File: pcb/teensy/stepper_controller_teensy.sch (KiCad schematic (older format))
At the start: 22 parts

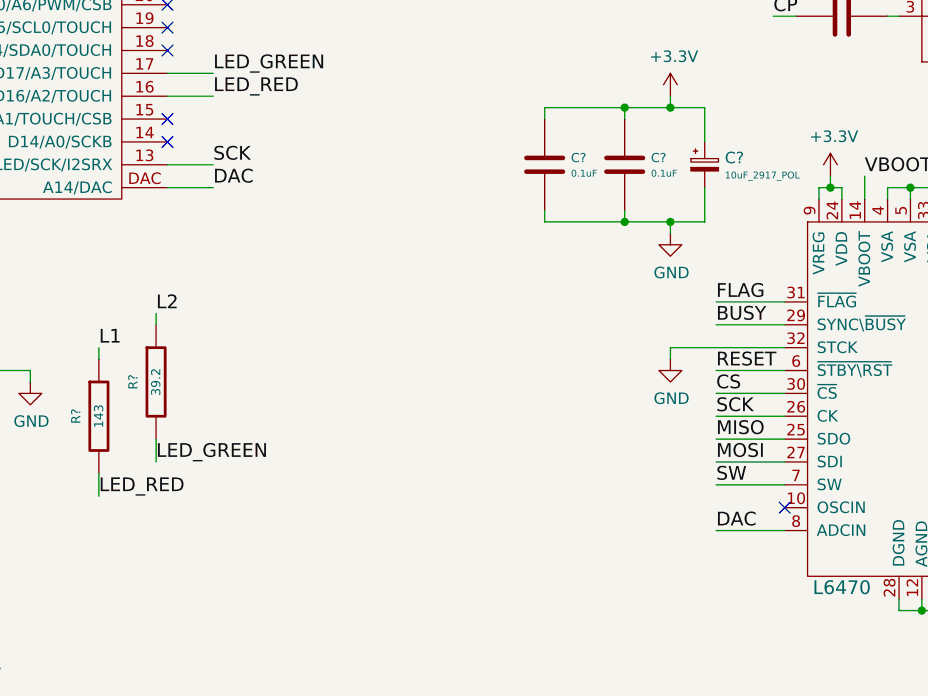
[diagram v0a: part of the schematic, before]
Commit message: Added component and made changes.
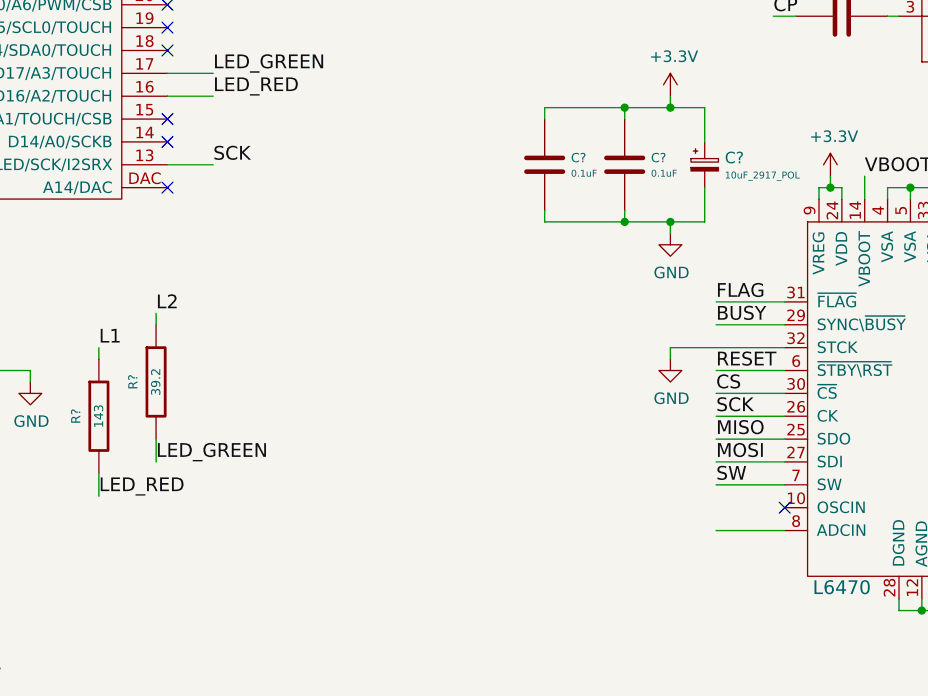
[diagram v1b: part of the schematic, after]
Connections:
- net DAC: no longer names the net of MDT?.DAC (A14/DAC)
- net DAC: no longer U?.8 (ADCIN)
- no-connect marks 20 -> 21
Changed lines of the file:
@@
 $EndComp
 Wire Wire Line
-	3850 2350 4050 2350
-Text Label 4050 2350 0    60   ~ 0
-DAC
-Wire Wire Line
 	6550 3850 6250 3850
-Text Label 6250 3850 0    60   ~ 0
-DAC
+NoConn ~ 3850 2350
 $EndSCHEMATC

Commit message: Progress towards pcb v1.0.
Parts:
- removed D?: diode_schottky_45V_10A, stepper_controller_teensy:CFP15, symbol diode_schottky_45V_10A
- removed P?: TERM_BLK_ANG_4_PIN_0.2_PITCH, stepper_controller_teensy:TERM_BLK_ANG_4_PIN_0.2_PITCH, symbol TERM_BLK_ANG_4_PIN_0.2_PITCH
- removed P?: PWR_JACK_2.5x5.5, stepper_controller_teensy:DCJACK_2PIN_HIGHCURRENT, symbol PWR_JACK_2.5x5.5
- removed T?: TERM_BLK_2_PIN_0.1_PITCH, stepper_controller_teensy:TERM_BLK_2_PIN_0.1_PITCH, symbol TERM_BLK_2_PIN_0.1_PITCH
- added C8: 0.1uF, stepper_controller_teensy:SM1210, symbol 0.1uF
- added T1: TERM_BLK_ANG_4_PIN_0.2_PITCH, footprints:TERM_BLK_ANG_4_PIN_0.2_PITCH, symbol TERM_BLK_ANG_4_PIN_0.2_PITCH
- added T2: TERM_BLK_ANG_2_PIN_0.2_PITCH, footprints:TERM_BLK_ANG_2_PIN_0.2_PITCH, symbol TERM_BLK_ANG_2_PIN_0.2_PITCH
- added TP1: TESTPOINT_RED, footprints:TESTPOINT_THRU, symbol TESTPOINT_RED
- added TP2, TP4: TESTPOINT_BLK, footprints:TESTPOINT_THRU, symbol TESTPOINT_BLK
- added TP3: TESTPOINT_WHT, footprints:TESTPOINT_THRU, symbol TESTPOINT_WHT
- added U3: CUR_SEN_+/-5A, footprints:SOIC_8_LC, symbol CUR_SEN_+/-5A
- gave numbers to parts that had none: 18
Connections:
- net +3V3: now also C8.1, U3.6 (BW_SEL), U3.8 (VCC)
- net GND: now also U1.8 (ADCIN), C8.2, T2.2 (P2), TP2.1, TP4.1, U3.5 (GND)
- net OUT1A: now also T1.1 (P1), U3.3 (IP-), U3.4 (IP-); no longer U1.2 (OUT1A), U1.3 (OUT1A)
- net OUT1B: now also T1.3 (P3)
- net OUT2A: now also T1.2 (P2)
- net OUT2B: now also T1.4 (P4)
- net SW_B: now also T2.1 (P1)
- net VDD: now also TP1.1
- net VIOUT: now reaches MDT1.14 (D14/A0/SCKB)
- net VIOUT: now also TP3.1, U3.7 (VIOUT)
- new net OUT1A_0: U1.2 (OUT1A), U1.3 (OUT1A), U3.1 (IP+), U3.2 (IP+)
- no-connect marks 21 -> 20

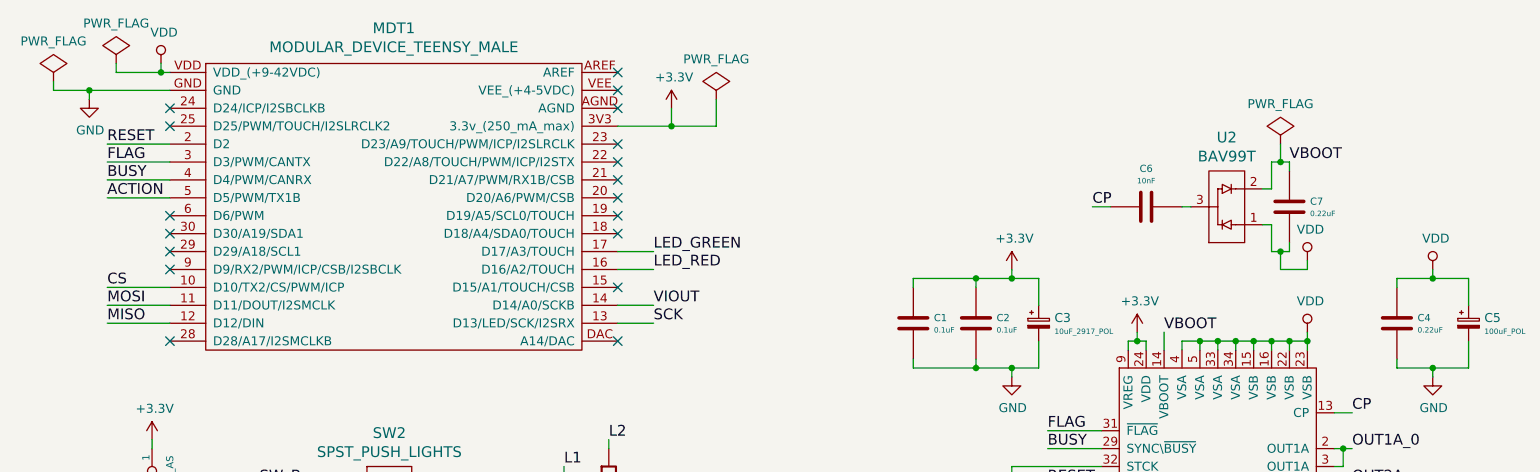
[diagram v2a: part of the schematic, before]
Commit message: Finished teensy pcb v1.0.
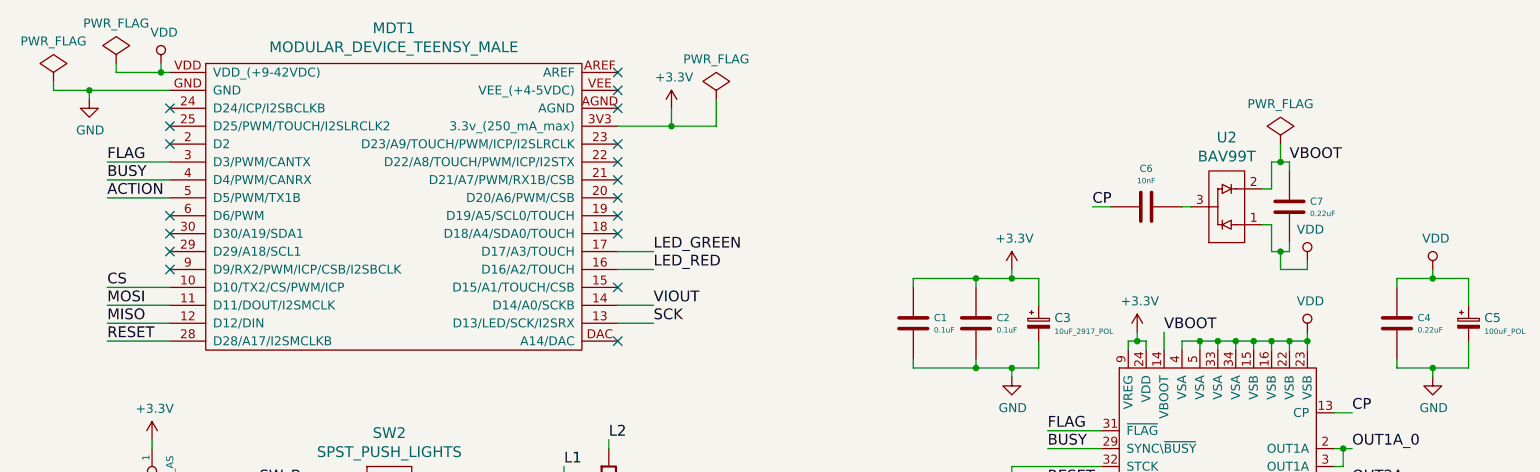
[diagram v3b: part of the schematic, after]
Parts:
- C4, C7: Description 0.22µF 100V Ceramic Capacitor X7R 1210 -> 0.22uF 100V Ceramic Capacitor X7R 1210
- C5: Description 100µF 100V Aluminum Capacitors Radial Can SMD -> 100uF 100V Aluminum Capacitors Radial Can SMD
- T1: footprint footprints:TERM_BLK_ANG_4_PIN_0.2_PITCH -> stepper_controller_teensy:TERM_BLK_ANG_4_PIN_0.2_PITCH
- T2: footprint footprints:TERM_BLK_ANG_2_PIN_0.2_PITCH -> stepper_controller_teensy:TERM_BLK_ANG_2_PIN_0.2_PITCH
- TP1, TP2, TP3, TP4: footprint footprints:TESTPOINT_THRU -> stepper_controller_teensy:TESTPOINT_THRU
- U3: footprint footprints:SOIC_8_LC -> stepper_controller_teensy:SOIC_8_LC
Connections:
- net GND: now also C4.2; no longer C4.1
- net RESET: now also MDT1.28 (D28/A17/I2SMCLKB); no longer MDT1.2 (D2)
- net VBOOT: now also C7.1; no longer C7.2
- net VDD: now also C4.1, C7.2; no longer C4.2, C7.1
